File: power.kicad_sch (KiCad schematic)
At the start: 95 parts, among them J7 USB-C_GCT_USB4105-GF-A, J8 Molex_Nano-Fit_1x2_SMD_105430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, Q3 2N7002_SOT-23-3, U10 TPS566231P, U14 TPS566231P, U15 TPS566231P, U16 TPS566231P, U17 TPS566231P

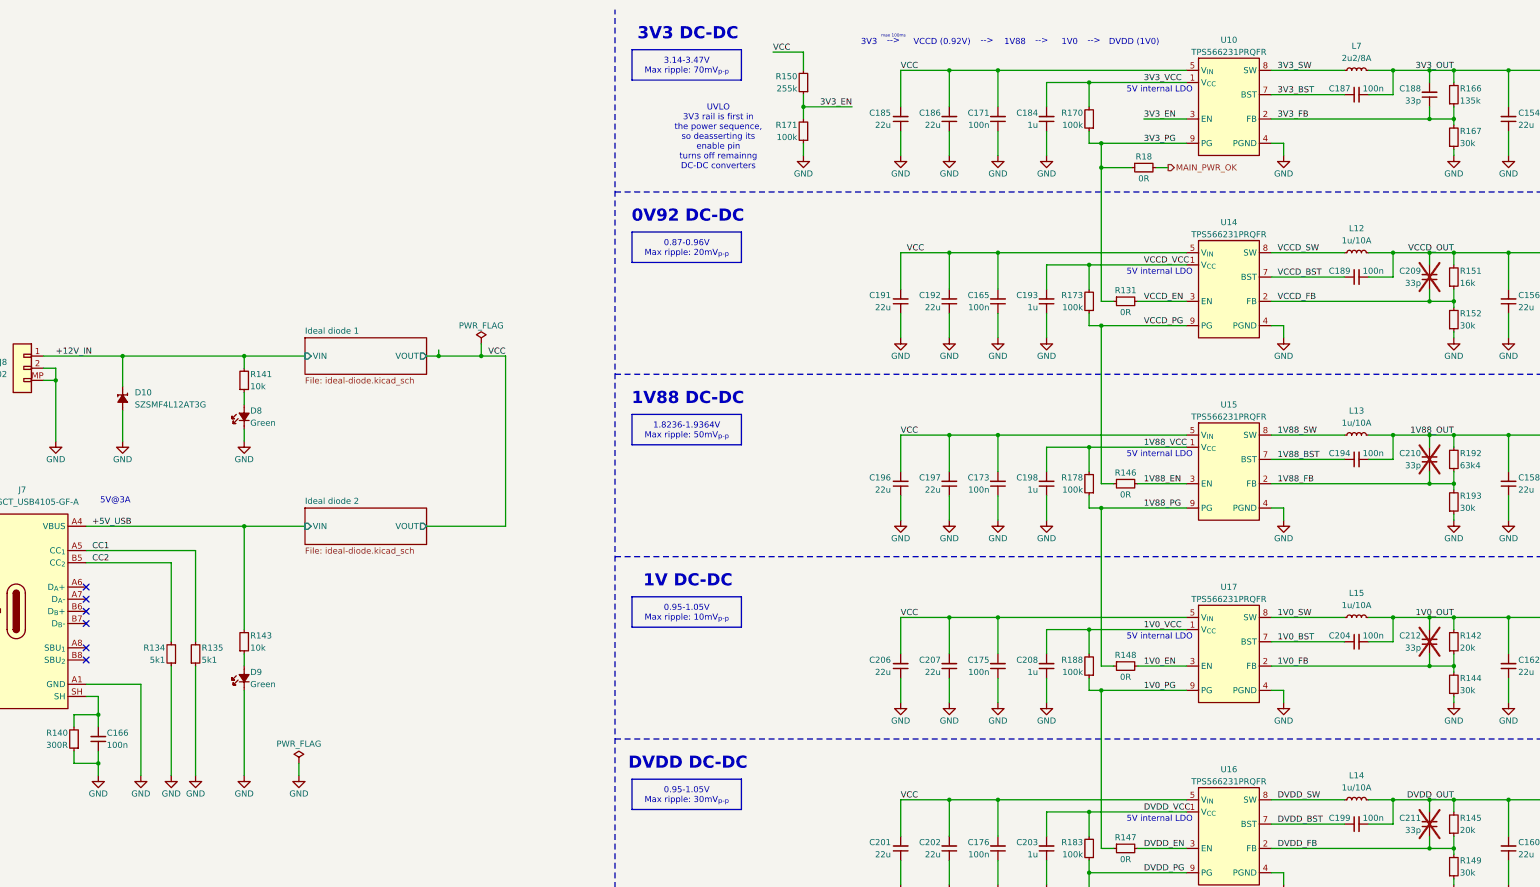
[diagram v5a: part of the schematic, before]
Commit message: [#85196] Clear ERC, minor schematic fixes
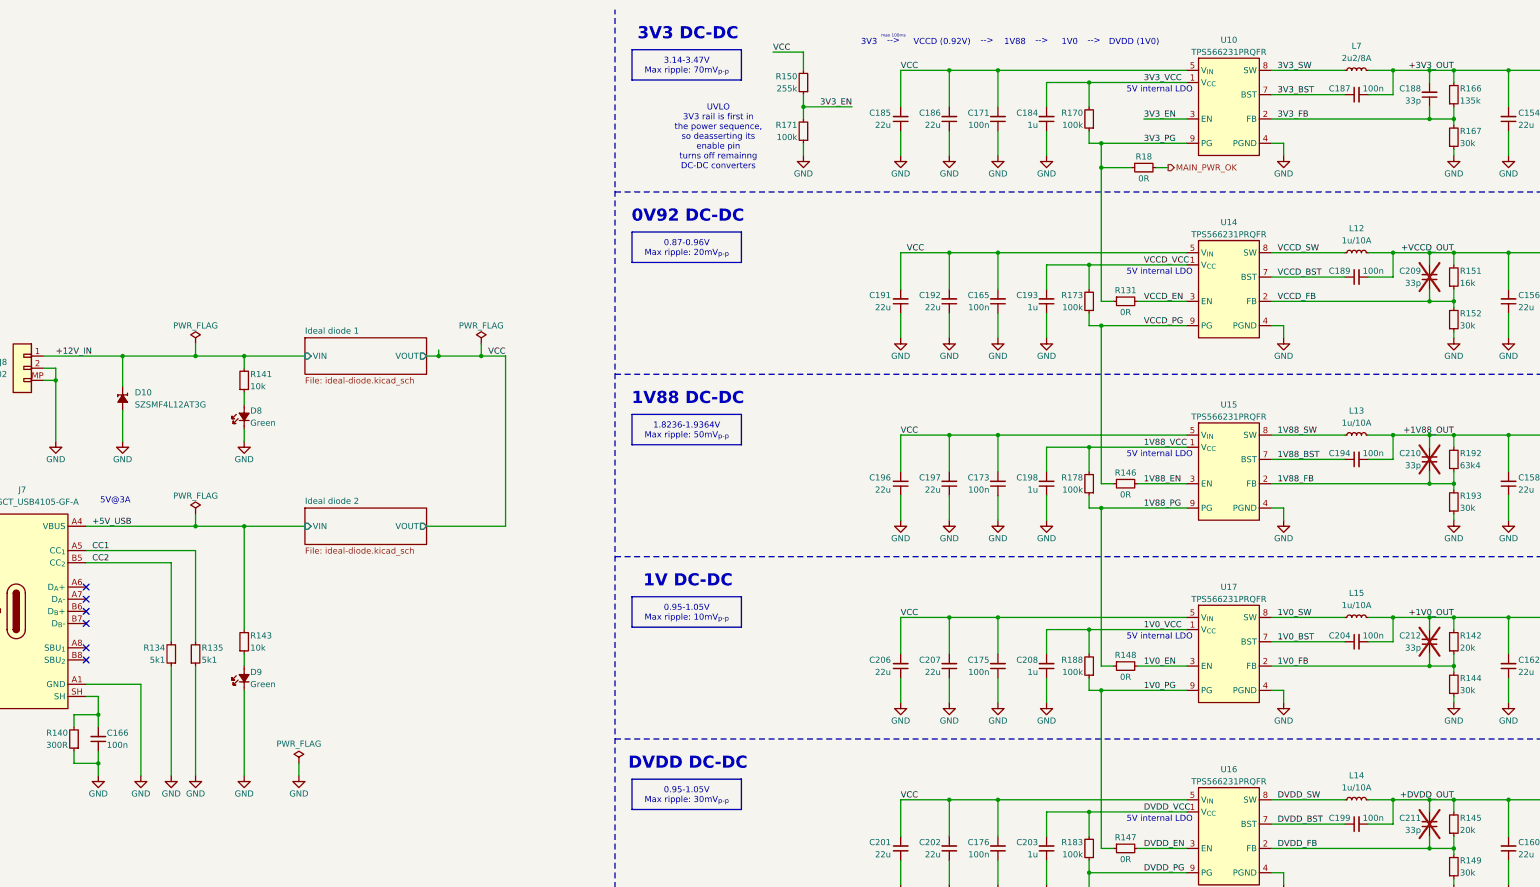
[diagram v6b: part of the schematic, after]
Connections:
- net 1V0_OUT renamed +1V0_OUT
- net 1V88_OUT renamed +1V88_OUT
- net 3V3_OUT renamed +3V3_OUT
- net DVDD_OUT renamed +DVDD_OUT
- net VCCD_OUT renamed +VCCD_OUT
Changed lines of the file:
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@@
 	)
 	(junction
+		(at 80.01 85.09)
+		(diameter 0)
+		(color 0 0 0 0)
+	)
+	(junction
 		(at 269.24 116.84)
 		(diameter 0)
@@
 	)
 	(junction
+		(at 80.01 120.65)
+		(diameter 0)
+		(color 0 0 0 0)
+	)
+	(junction
 		(at 50.8 90.17)
 		(diameter 0)
@@
 	(wire
 		(pts
+			(xy 80.01 118.11) (xy 80.01 120.65)
+		)
+		(stroke
+			(width 0)
+			(type default)
+		)
+	)
+	(wire
+		(pts
 			(xy 227.33 101.6) (xy 237.49 101.6)
 		)
@@
 	(wire
 		(pts
+			(xy 80.01 82.55) (xy 80.01 85.09)
+		)
+		(stroke
+			(width 0)
+			(type default)
+		)
+	)
+	(wire
+		(pts
 			(xy 128.27 85.09) (xy 130.81 85.09)
 		)
@@
 	(wire
 		(pts
+			(xy 80.01 85.09) (xy 90.17 85.09)
+		)
+		(stroke
+			(width 0)
+			(type default)
+		)
+	)
+	(wire
+		(pts
 			(xy 391.16 99.06) (xy 391.16 101.6)
 		)
@@
 	(wire
 		(pts
-			(xy 64.77 85.09) (xy 90.17 85.09)
+			(xy 64.77 85.09) (xy 80.01 85.09)
 		)
 		(stroke
@@
 		)
 	)
+	(wire
+		(pts
+			(xy 80.01 120.65) (xy 90.17 120.65)
+		)
+		(stroke
+			(width 0)
+			(type default)
+		)
+	)
 	(polyline
 		(pts
@@
 	(wire
 		(pts
-			(xy 57.15 120.65) (xy 90.17 120.65)
+			(xy 57.15 120.65) (xy 80.01 120.65)
 		)
 		(stroke
@@
 		)
 	)
-	(label "DVDD_OUT"
+	(label "+DVDD_OUT"
 		(at 342.9 177.8 180)
 		(effects
@@
 		)
 	)
-	(label "VCCD_OUT"
+	(label "+VCCD_OUT"
 		(at 342.9 63.5 180)
 		(effects
@@
 		)
 	)
-	(label "3V3_OUT"
+	(label "+3V3_OUT"
 		(at 342.9 25.4 180)
 		(effects
@@
 		)
 	)
-	(label "1V0_OUT"
+	(label "+1V0_OUT"
 		(at 342.9 139.7 180)
 		(effects
@@
 		)
 	)
-	(label "1V88_OUT"
+	(label "+1V88_OUT"
 		(at 342.9 101.6 180)
 		(effects
@@
 	)
 	(symbol
+		(lib_id "antmicropower:PWR_FLAG")
+		(at 80.01 82.55 0)
+		(unit 1)
+		(exclude_from_sim no)
+		(in_bom yes)
+		(on_board yes)
+		(dnp no)
+		(property "Reference" "#FLG02"
+			(at 80.01 80.645 0)
+			(effects
+				(font
+					(size 1.27 1.27)
+				)
+				(hide yes)
+			)
+		)
+		(property "Value" "PWR_FLAG"
+			(at 80.01 78.74 0)
+			(effects
+				(font
+					(size 1.27 1.27)
+				)
+			)
+		)
+		(property "Footprint" ""
+			(at 80.01 82.55 0)
+			(effects
+				(font
+					(size 1.27 1.27)
+				)
+				(hide yes)
+			)
+		)
+		(property "Datasheet" ""
+			(at 80.01 82.55 0)
+			(effects
+				(font
+					(size 1.27 1.27)
+				)
+				(hide yes)
+			)
+		)
+		(property "Description" ""
+			(at 80.01 82.55 0)
+			(effects
+				(font
+					(size 1.27 1.27)
+				)
+				(hide yes)
+			)
+		)
+		(pin "1"
+		)
+		(instances
+			(project "10-gbe-expansion"
+				(path "/04bda987-e5eb-48b4-9e90-d8211dc11b39/3d913a88-b6f3-4148-9b3d-882d5df37282"
+					(reference "#FLG02")
+					(unit 1)
+				)
+			)
+		)
+	)
+	(symbol
 		(lib_id "antmicroDCDCConverters:TPS566231P")
 		(at 287.02 177.8 0)
@@
 					(unit 1)
 				)
+			)
+		)
+	)
+	(symbol
+		(lib_id "antmicropower:PWR_FLAG")
+		(at 80.01 118.11 0)
+		(unit 1)
+		(exclude_from_sim no)
+		(in_bom yes)
+		(on_board yes)
+		(dnp no)
+		(property "Reference" "#FLG01"
+			(at 80.01 116.205 0)
+			(effects
+				(font
+					(size 1.27 1.27)
+				)
+				(hide yes)
+			)
+		)
+		(property "Value" "PWR_FLAG"
+			(at 80.01 114.3 0)
+			(effects
+				(font
+					(size 1.27 1.27)
+				)
+			)
+		)
+		(property "Footprint" ""
+			(at 80.01 118.11 0)
+			(effects
+				(font
+					(size 1.27 1.27)
+				)
+				(hide yes)
+			)
+		)
+		(property "Datasheet" ""
+			(at 80.01 118.11 0)
+			(effects
+				(font
+					(size 1.27 1.27)
+				)
+				(hide yes)
+			)
+		)
+		(property "Description" ""
+			(at 80.01 118.11 0)
+			(effects
+				(font
+					(size 1.27 1.27)
+				)
+				(hide yes)
+			)
+		)
+		(pin "1"
+		)
+		(instances
+			(project "10-gbe-expansion"
+				(path "/04bda987-e5eb-48b4-9e90-d8211dc11b39/3d913a88-b6f3-4148-9b3d-882d5df37282"
+					(reference "#FLG01")
+					(unit 1)
+				)

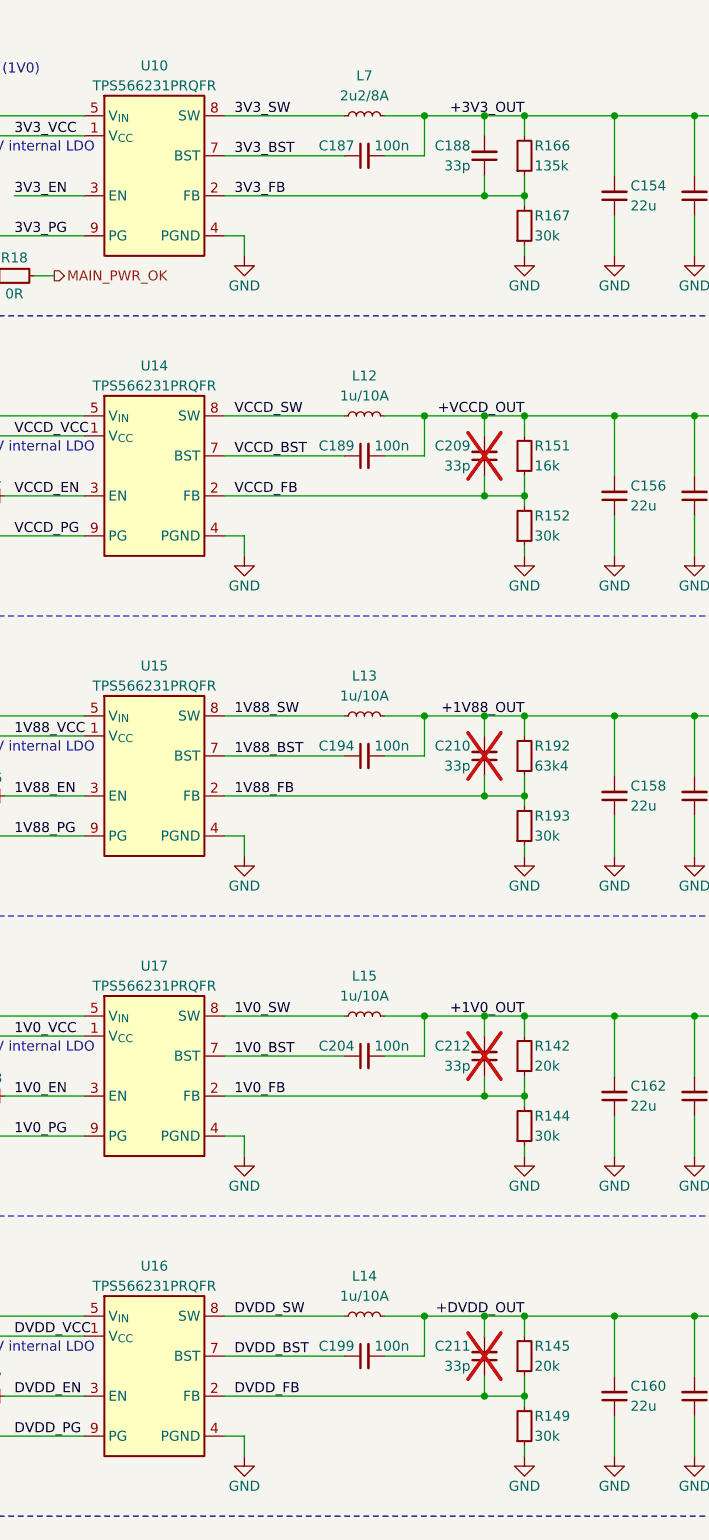
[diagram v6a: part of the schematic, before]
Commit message: [#85196] Fix bootstrap capacitor connections
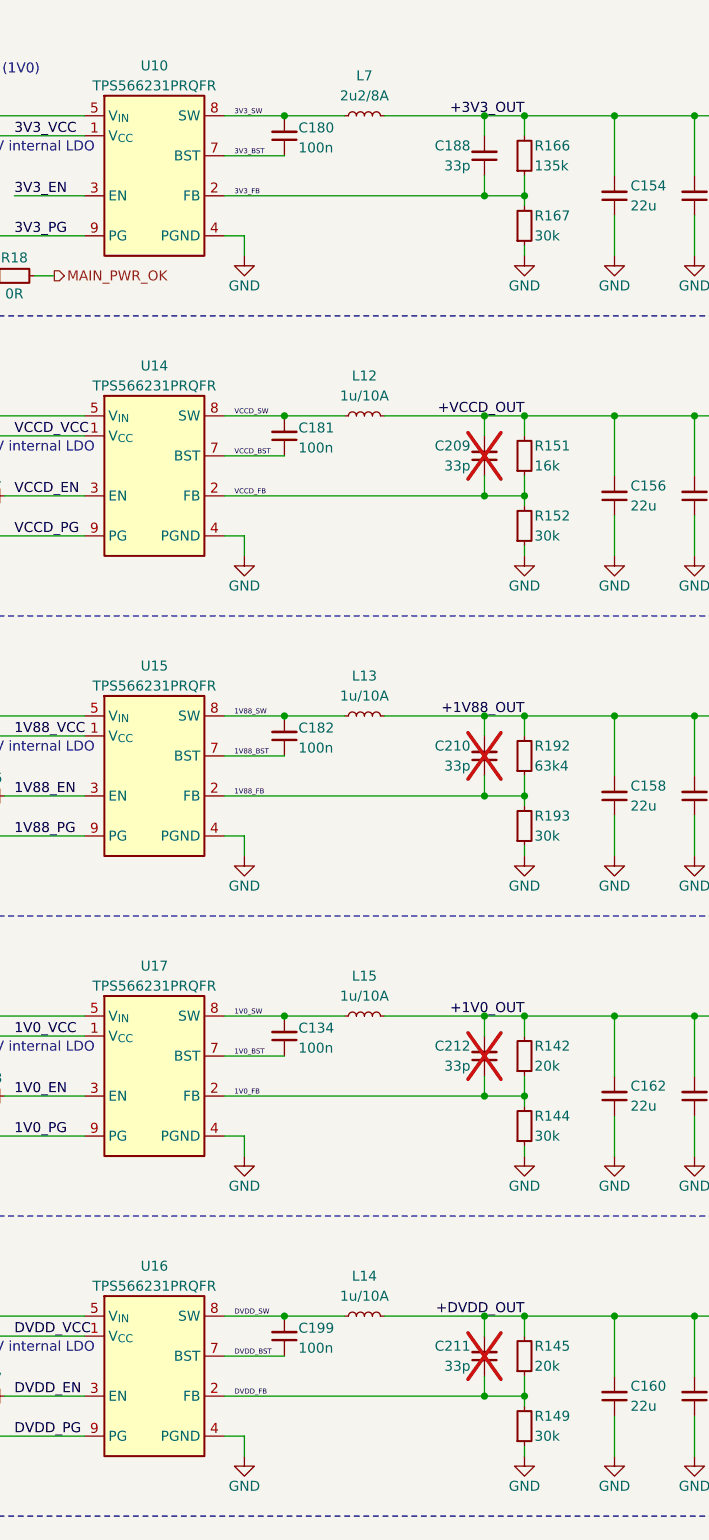
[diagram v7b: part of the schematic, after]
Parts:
- removed C187, C189, C194, C204: C_100n_0402, antmicro-footprints:C_0402_1005Metric, symbol antmicroCapacitors0402:C_100n_0402
- added C134, C180, C181, C182: C_100n_0402, antmicro-footprints:C_0402_1005Metric, symbol antmicroCapacitors0402:C_100n_0402
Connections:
- net +DVDD_OUT: no longer C199.2
- net 1V0_BST: now also C134.1
- net 1V0_SW: now also C134.2
- net 1V88_BST: now also C182.1
- net 1V88_SW: now also C182.2
- net 3V3_BST: now also C180.1
- net 3V3_SW: now also C180.2
- net DVDD_SW: now also C199.2
- net VCCD_BST: now also C181.1
- net VCCD_SW: now also C181.2
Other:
- moved on the sheet: C199

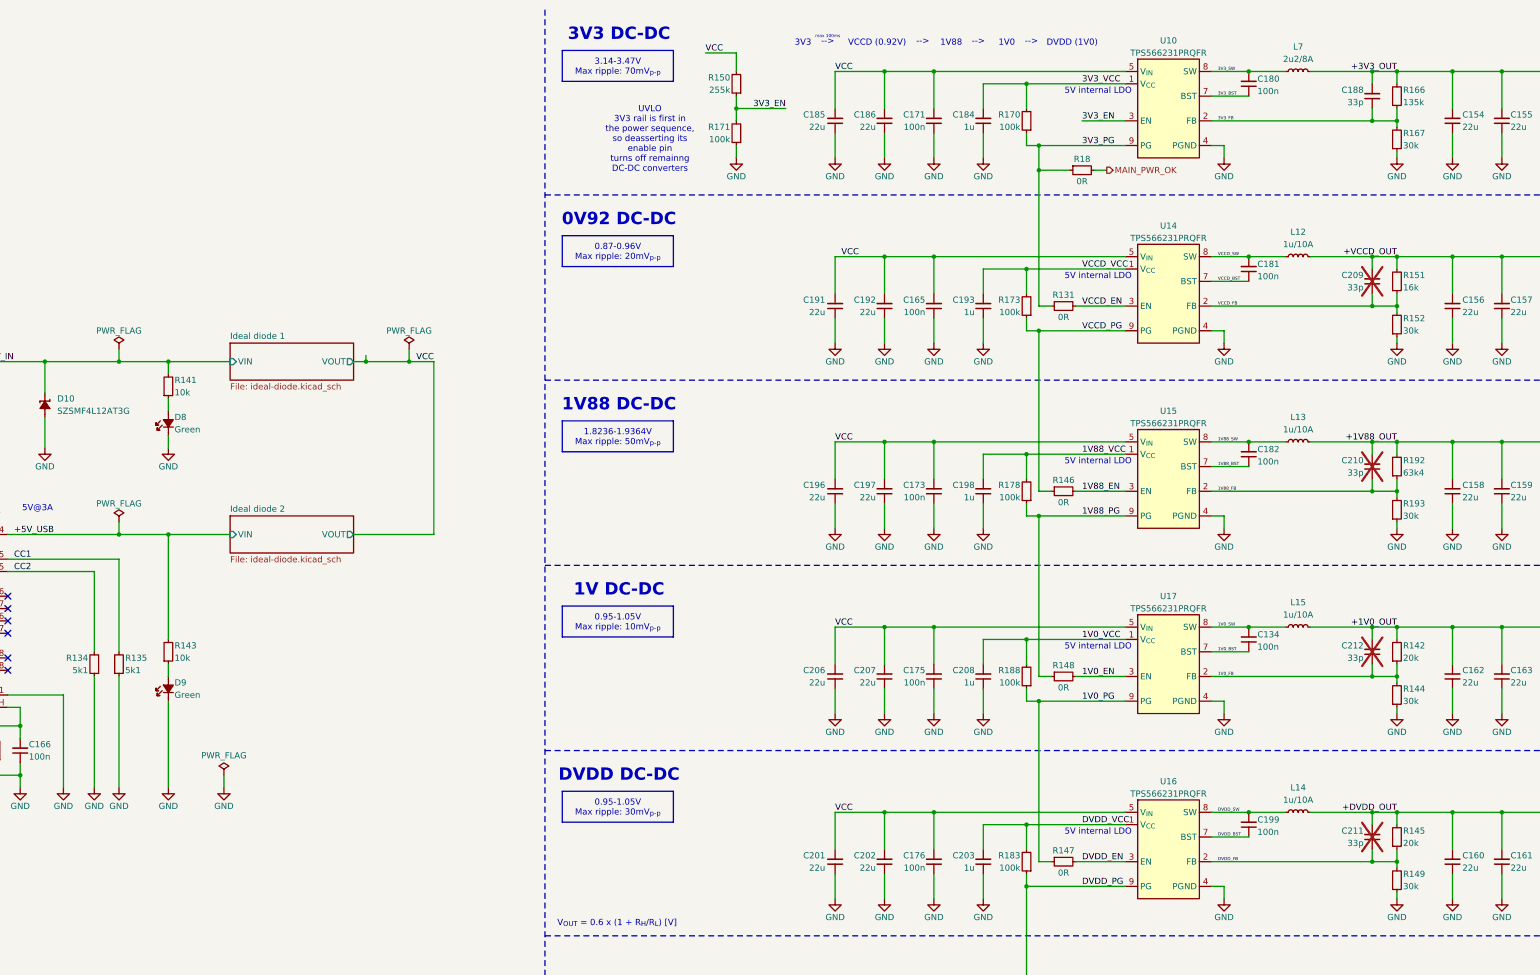
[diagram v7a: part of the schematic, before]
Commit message: [#85196] Change 2u2 inductor, minor schematic cleanup
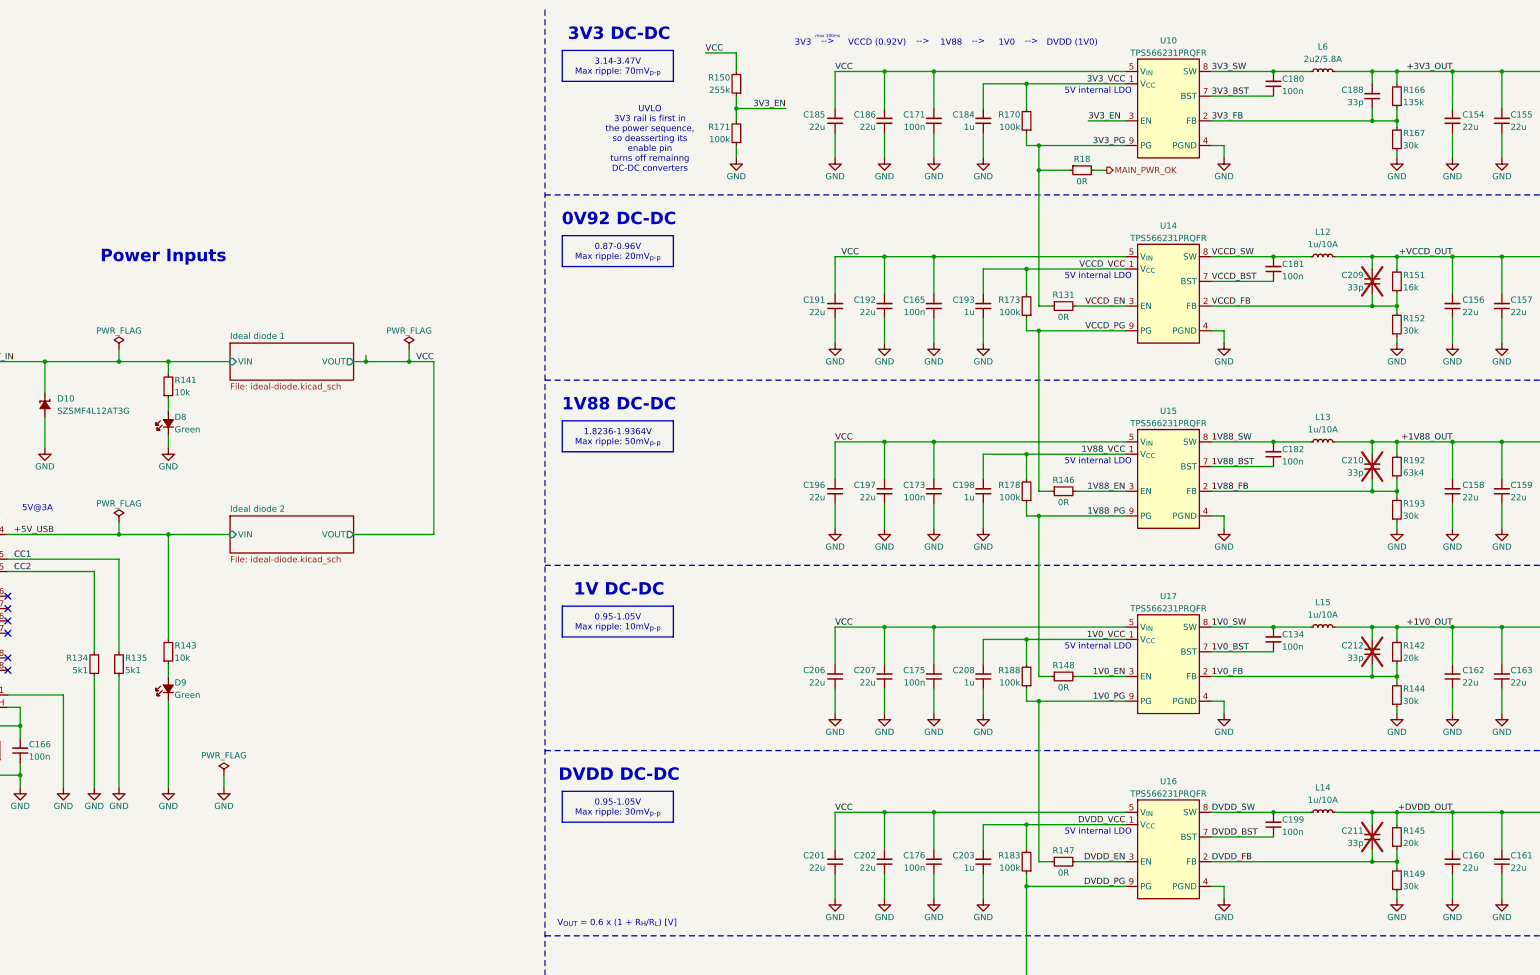
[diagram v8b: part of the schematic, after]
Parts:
- removed L7: L_2u2_8A_Coilcraft-XFL4020, antmicro-footprints:L_Coilcraft-XFL4020, symbol antmicroFixedInductors:L_2u2_8A_Coilcraft-XFL4020
- added L6: L_2u2_5.8A_WE-PMFI-35329222, antmicro-footprints:L_WE-PMFI-353220, symbol antmicroFixedInductors:L_2u2_5.8A_WE-PMFI-35329222
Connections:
- net +3V3_OUT: now also L6.2
- net 3V3_SW: now also L6.1
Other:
- note added: "Power Inputs"
- moved on the sheet: C134, C180, C181, C182, C199, L12, L13, L14, L15
